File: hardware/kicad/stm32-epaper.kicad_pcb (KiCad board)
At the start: 4 copper layers, 97.4 x 60 mm, 156 parts, among them J1 USB_C_Receptacle_USB2.0_16P, J101 TC2050-IDC-NL, J102 UART (TX RX GND), J2 BATT (1S LiPo), J201 microSD, J301 IT8951 HAT, J302 Electrodes L, J303 Electrodes R, SW101 BOOT, SW301 PEC11R-4220F-S0024, SW302 POWER, U1 BQ24073RGT, U101 STM32F469IIT6, U2 TPS63802DLA, U201 IS42S16400J-6TLI, U202 W25Q128JVSIQ, U3 TPS61023DRL, U301 CAP1188-1-CP-TR, U302 TPD2E2U06DCKR, U303 TPD2E2U06DCKR, U4 TPS22965DSG, U5 USBLC6-2SC6, U6 TPS63900DSK, U7 MCP1700T-3002E/TT, Y101 8MHz CL8pF, Y102 32.768kHz CL6pF

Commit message: Board: Michael's routing in KiCad (0 unconnected); schematic pilot: I2C pull-ups wired on the MCU sheet
- stm32-epaper.kicad_pcb as saved from KiCad 2026-09-24 07:39 (last two
  connections routed by hand: DRC 0 unconnected), footprints re-linked to the
  redrawn schematic (R304/R305 -> R105/R106) by sync_board_to_schematic.py.
- Schematic pilot: I2C1 pull-ups drawn wired to PB8/PB9 with junctions
  (moved from the Peripherals sheet). compare_netlists.py: electrically
  identical (156 parts, 193 nets).

Co-Authored-By: Claude Opus 5.5 <noreply@anthropic.com>
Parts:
- moved C301 1.30 mm to (143.7, 101.2)
- moved R308 0.46 mm to (140.6, 103.8)
- renumbered R304 to R105, R305 to R106
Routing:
- net I2C1_SDA: track 20.4 -> 34.4 mm, vias 2 -> 4
- net GND: track 158.8 -> 165.1 mm, vias 155 -> 150
- net 3V3_AON: track 65.1 -> 67.5 mm
- net CAP_RESET: track 39.8 -> 40.5 mm

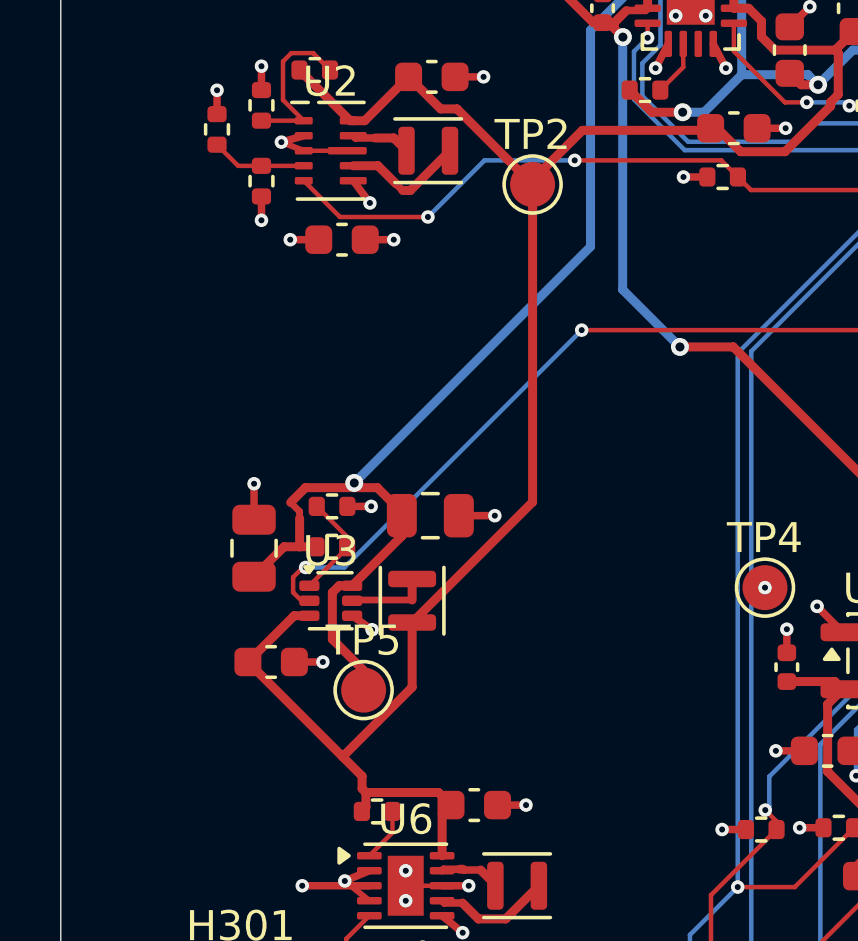
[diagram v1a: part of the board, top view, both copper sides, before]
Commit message: Board + project as finally saved from KiCad; footprints re-synced to the schematic
Michael's later routing edits and DRC exclusions for the power switch's
footprint hole clearances; R304/R305 -> R105/R106 re-applied by
sync_board_to_schematic.py. DRC: 0 unconnected, 0 parity issues.

Co-Authored-By: Claude Opus 5.5 <noreply@anthropic.com>
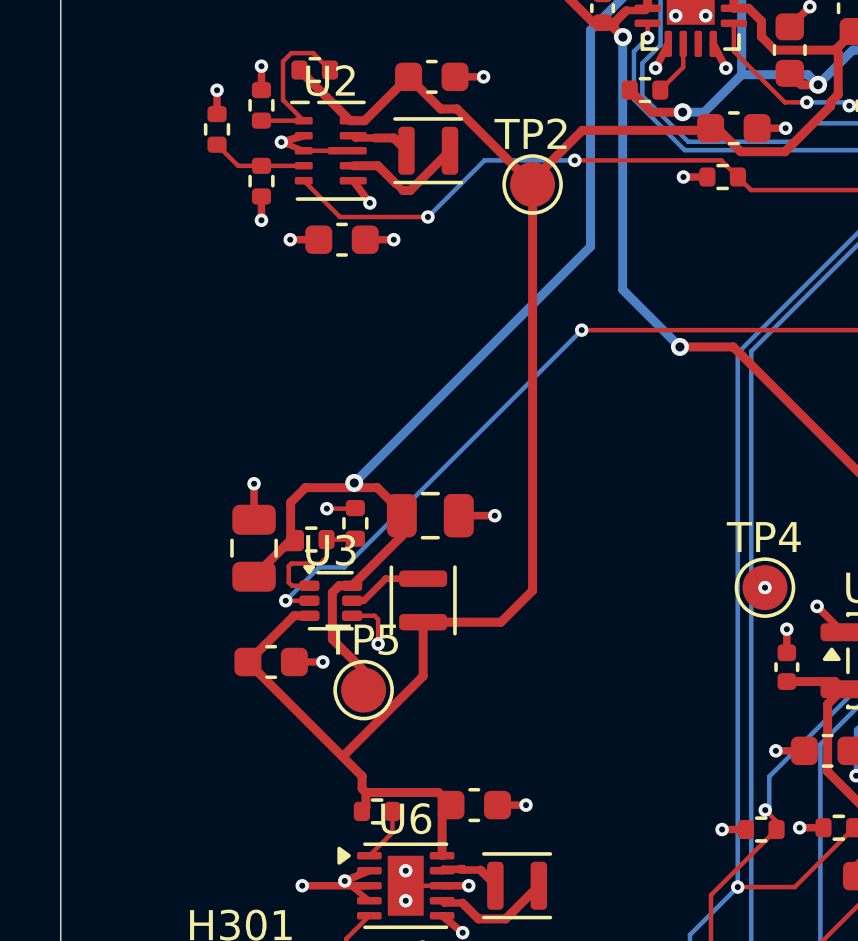
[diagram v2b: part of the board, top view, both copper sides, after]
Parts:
- moved R11 0.96 mm to (109.8, 131.4), turned to 90 degrees
- moved R10 0.73 mm to (108.3, 132.0)
- moved L2 0.37 mm to (112.1, 134.0)
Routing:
- net VSYS: track 66.1 -> 67.6 mm
- net GND: track 165.1 -> 166.2 mm
- net /Power/BST_FB: track 3.59 -> 4.26 mm
- net +5V: track 91.3 -> 90.7 mm
